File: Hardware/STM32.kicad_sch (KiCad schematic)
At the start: 10 parts, among them U22 MCU, STM32G0B0CETx

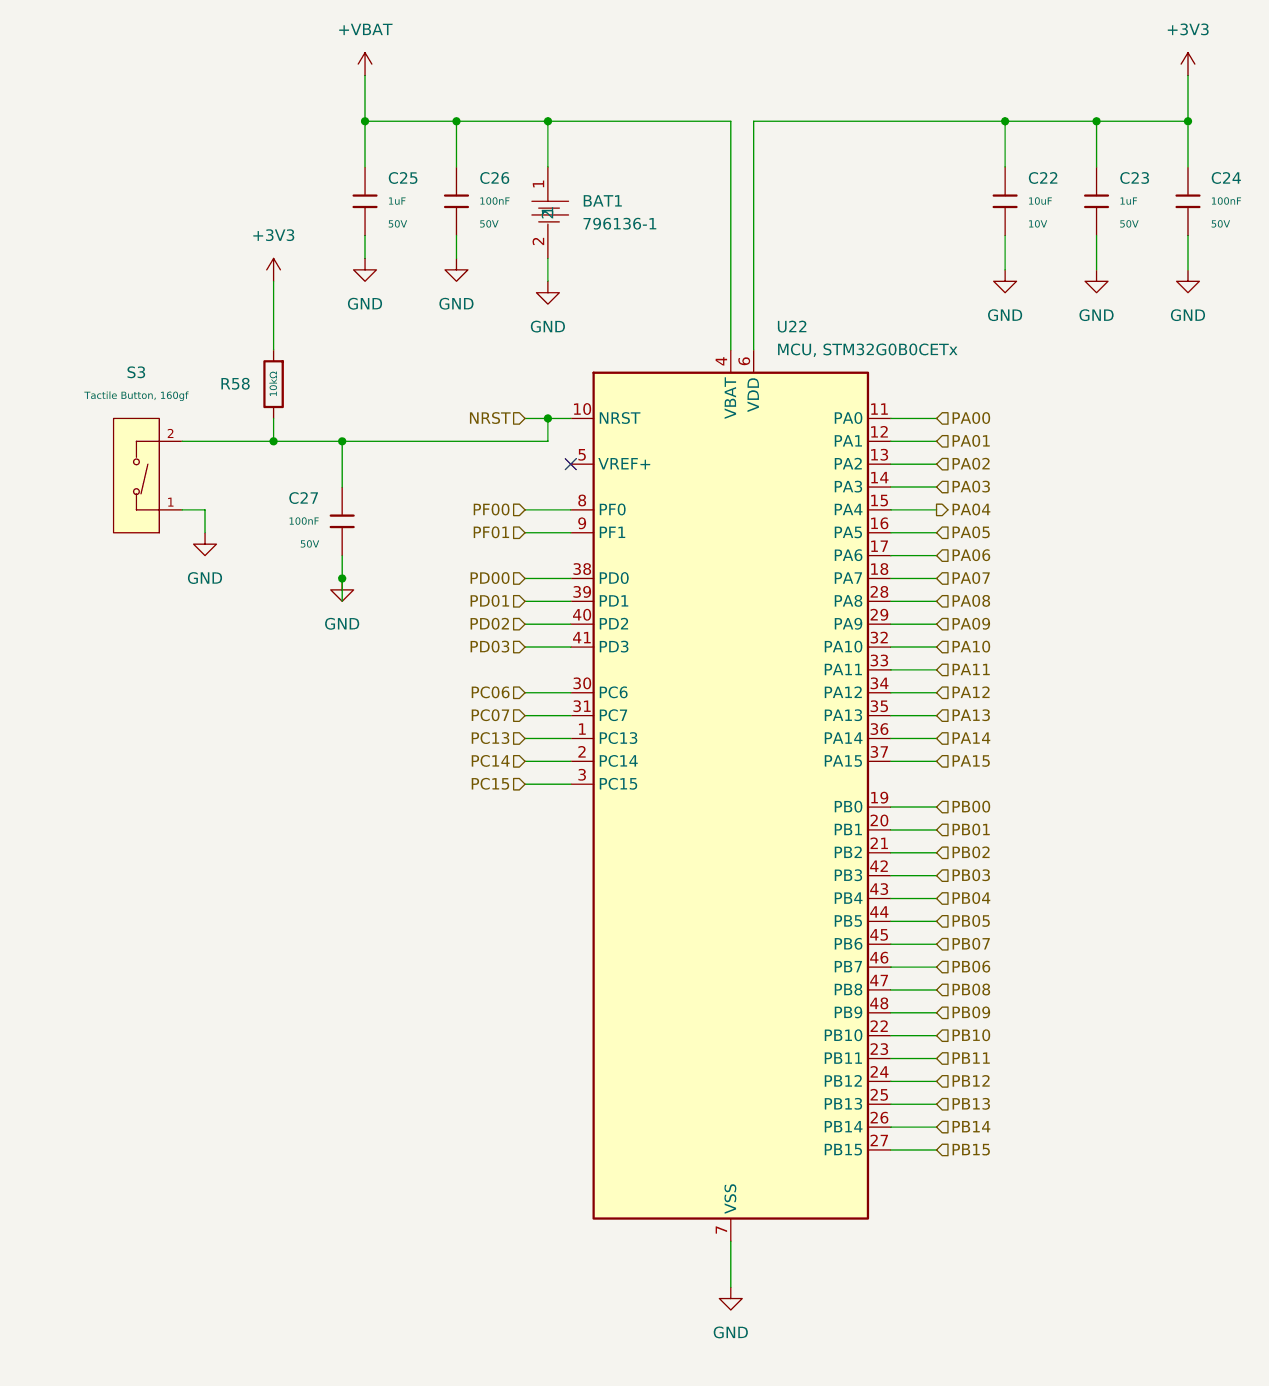
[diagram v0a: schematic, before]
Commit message: remove unused sheets
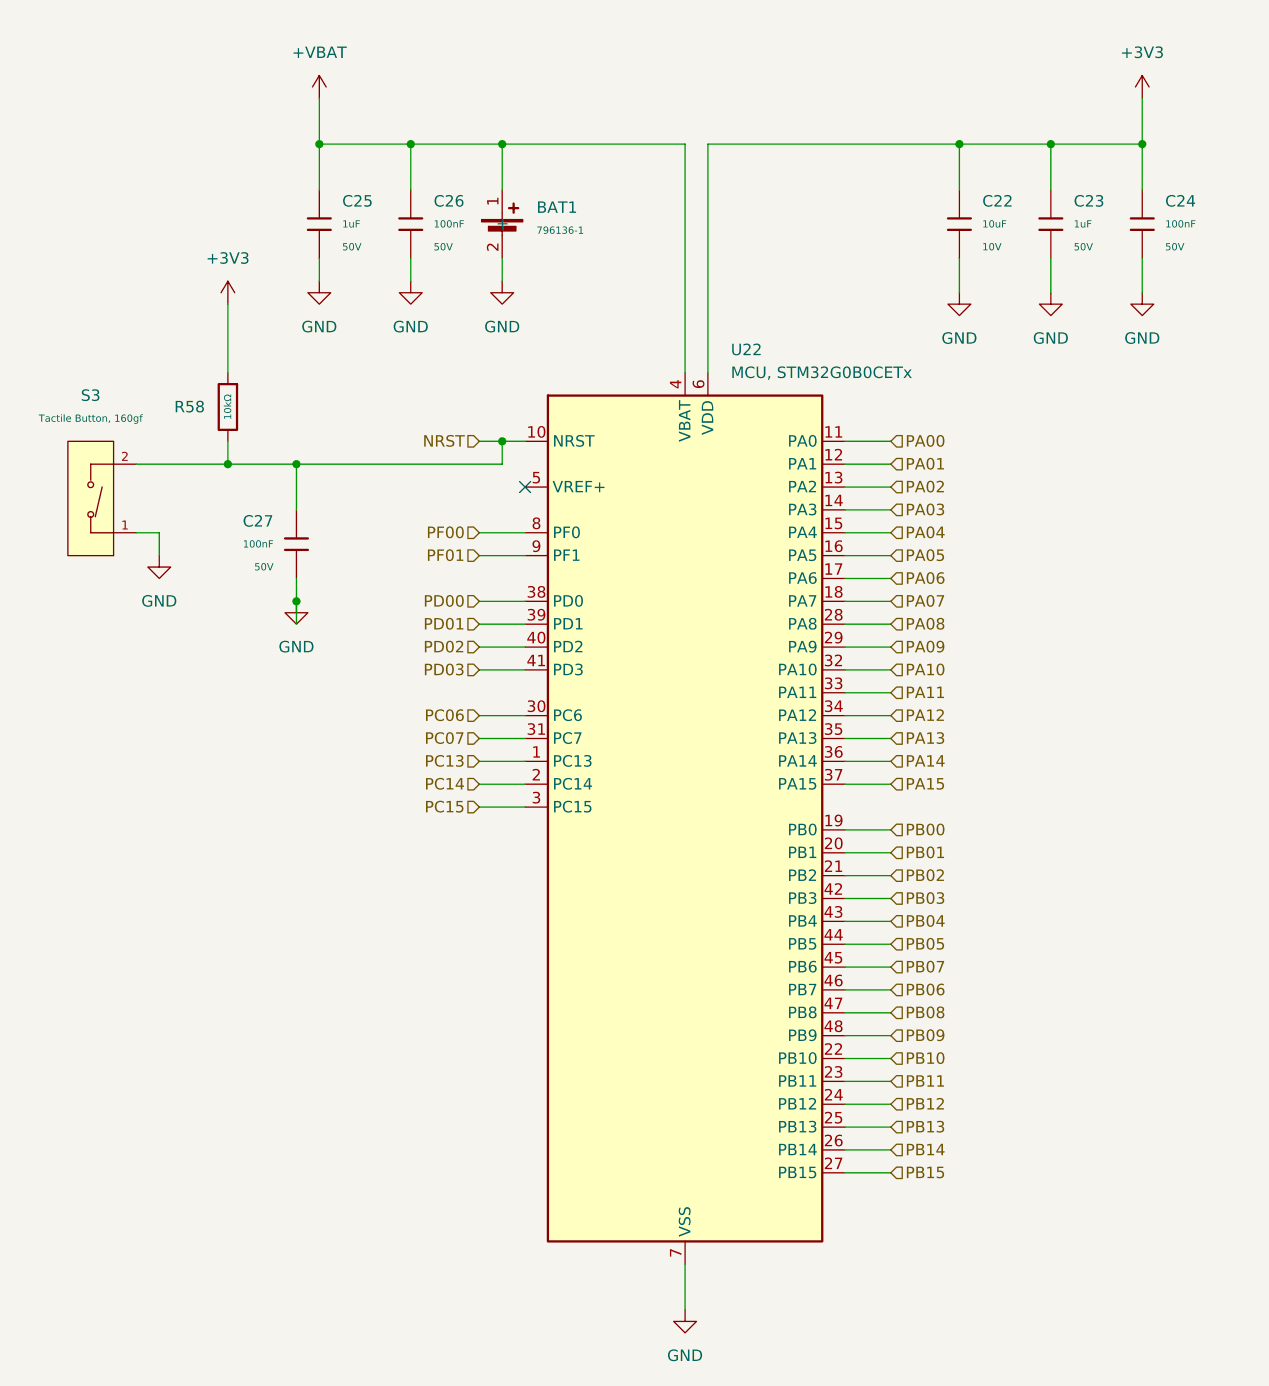
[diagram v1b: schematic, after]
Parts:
- removed BAT1: 796136-1, EasyEDA:BAT-SMD_796136-1, symbol EasyEDA:796136-1
- added BAT1: 796136-1, EASYEDA2KICAD:BAT-SMD_796136-1, symbol PCM_JLCPCB-Extended:BAT, COIN 2032
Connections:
- net +VBAT: now also BAT1.1 (+)
- net GND: now also BAT1.2 (-)
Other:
- moved on the sheet: C22, C23, C24, C25, C26, C27, R58, S3, U22
